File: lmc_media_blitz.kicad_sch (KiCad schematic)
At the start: 56 parts, among them J3 Conn_01x12, J4 Conn_01x12, Q1 BSS138W, Q2 BSS138W, SW1 SW_Push, SW2 SW_Push, SW3 SW_Push, U1 XC6206PxxxMR, U2 TPS613222ADBV, U3 STM32F030C8Tx

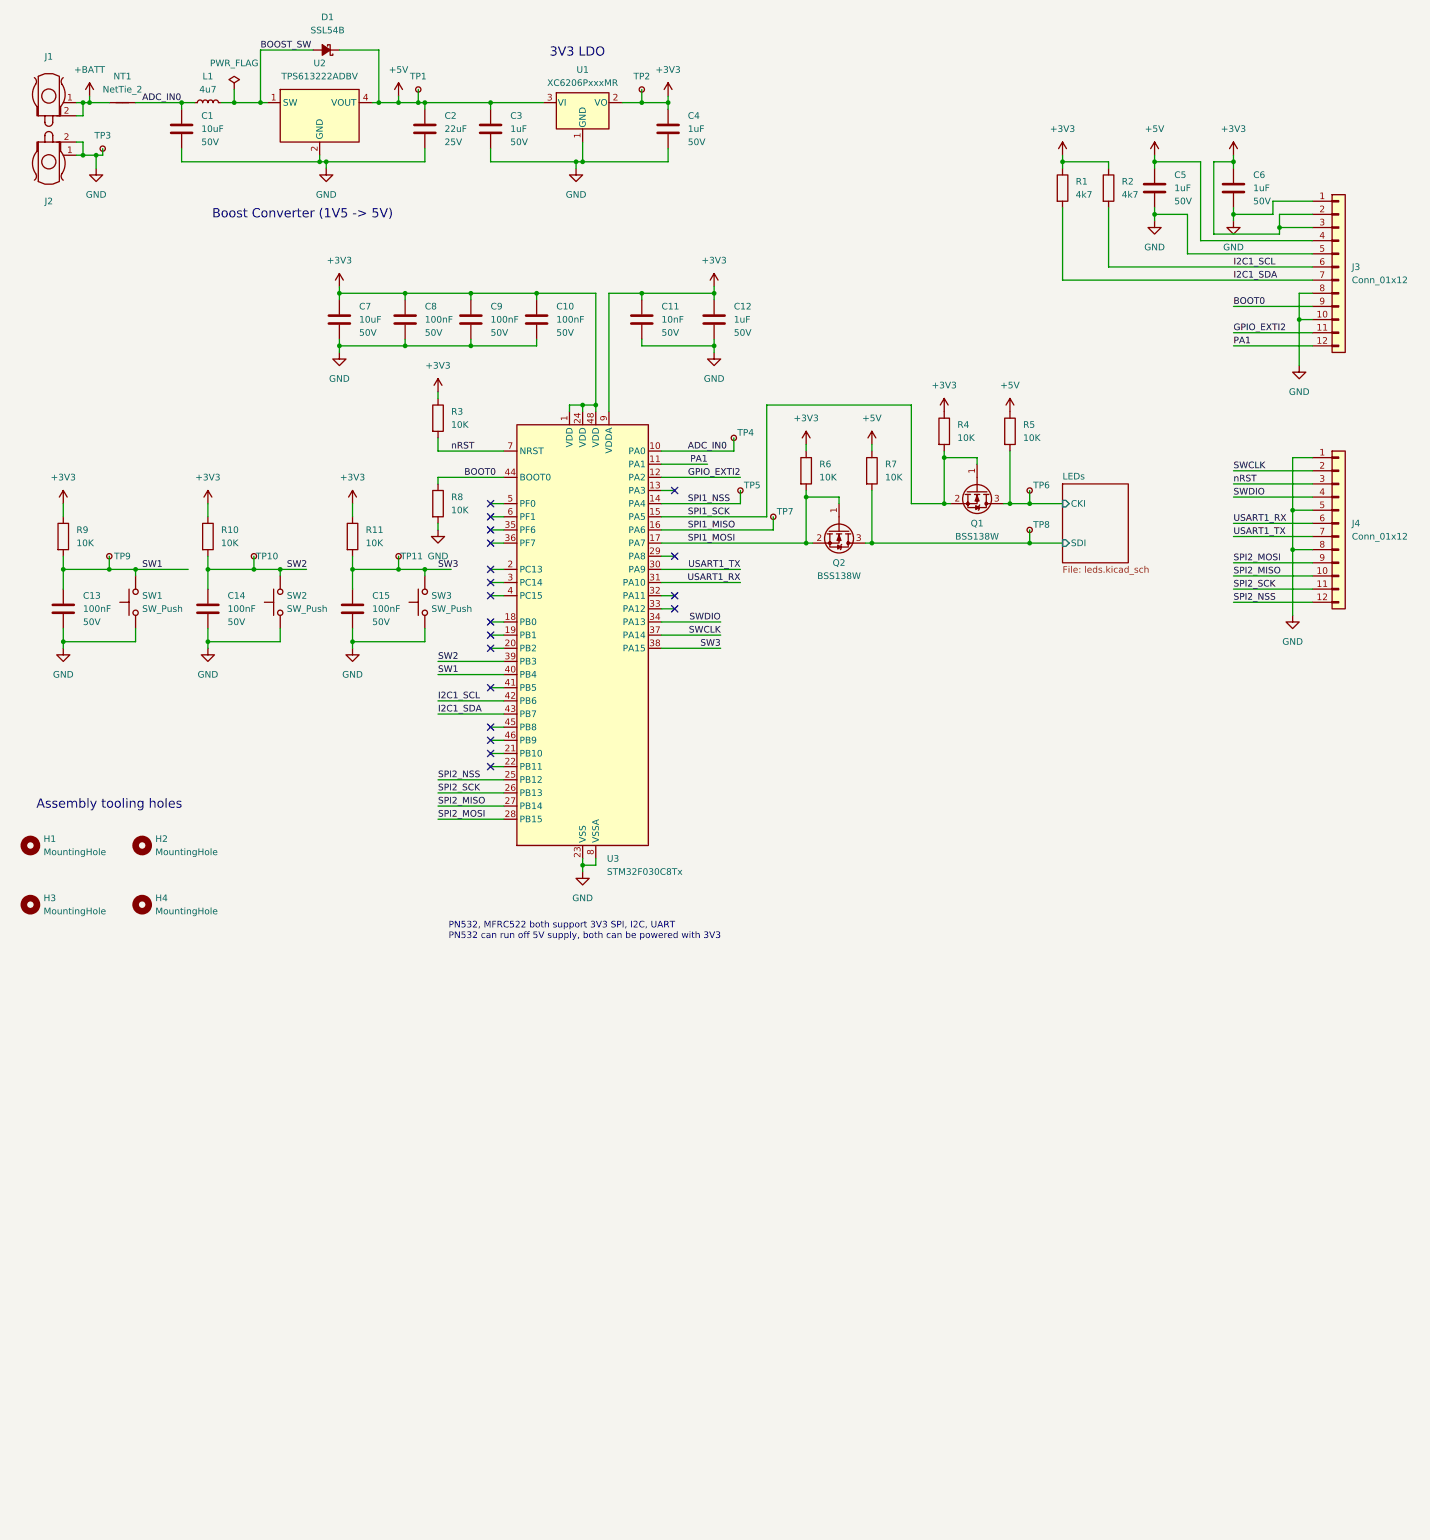
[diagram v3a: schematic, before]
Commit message: Changed 1x12 connectors to 2x12 connectors, and made board shape rectangular
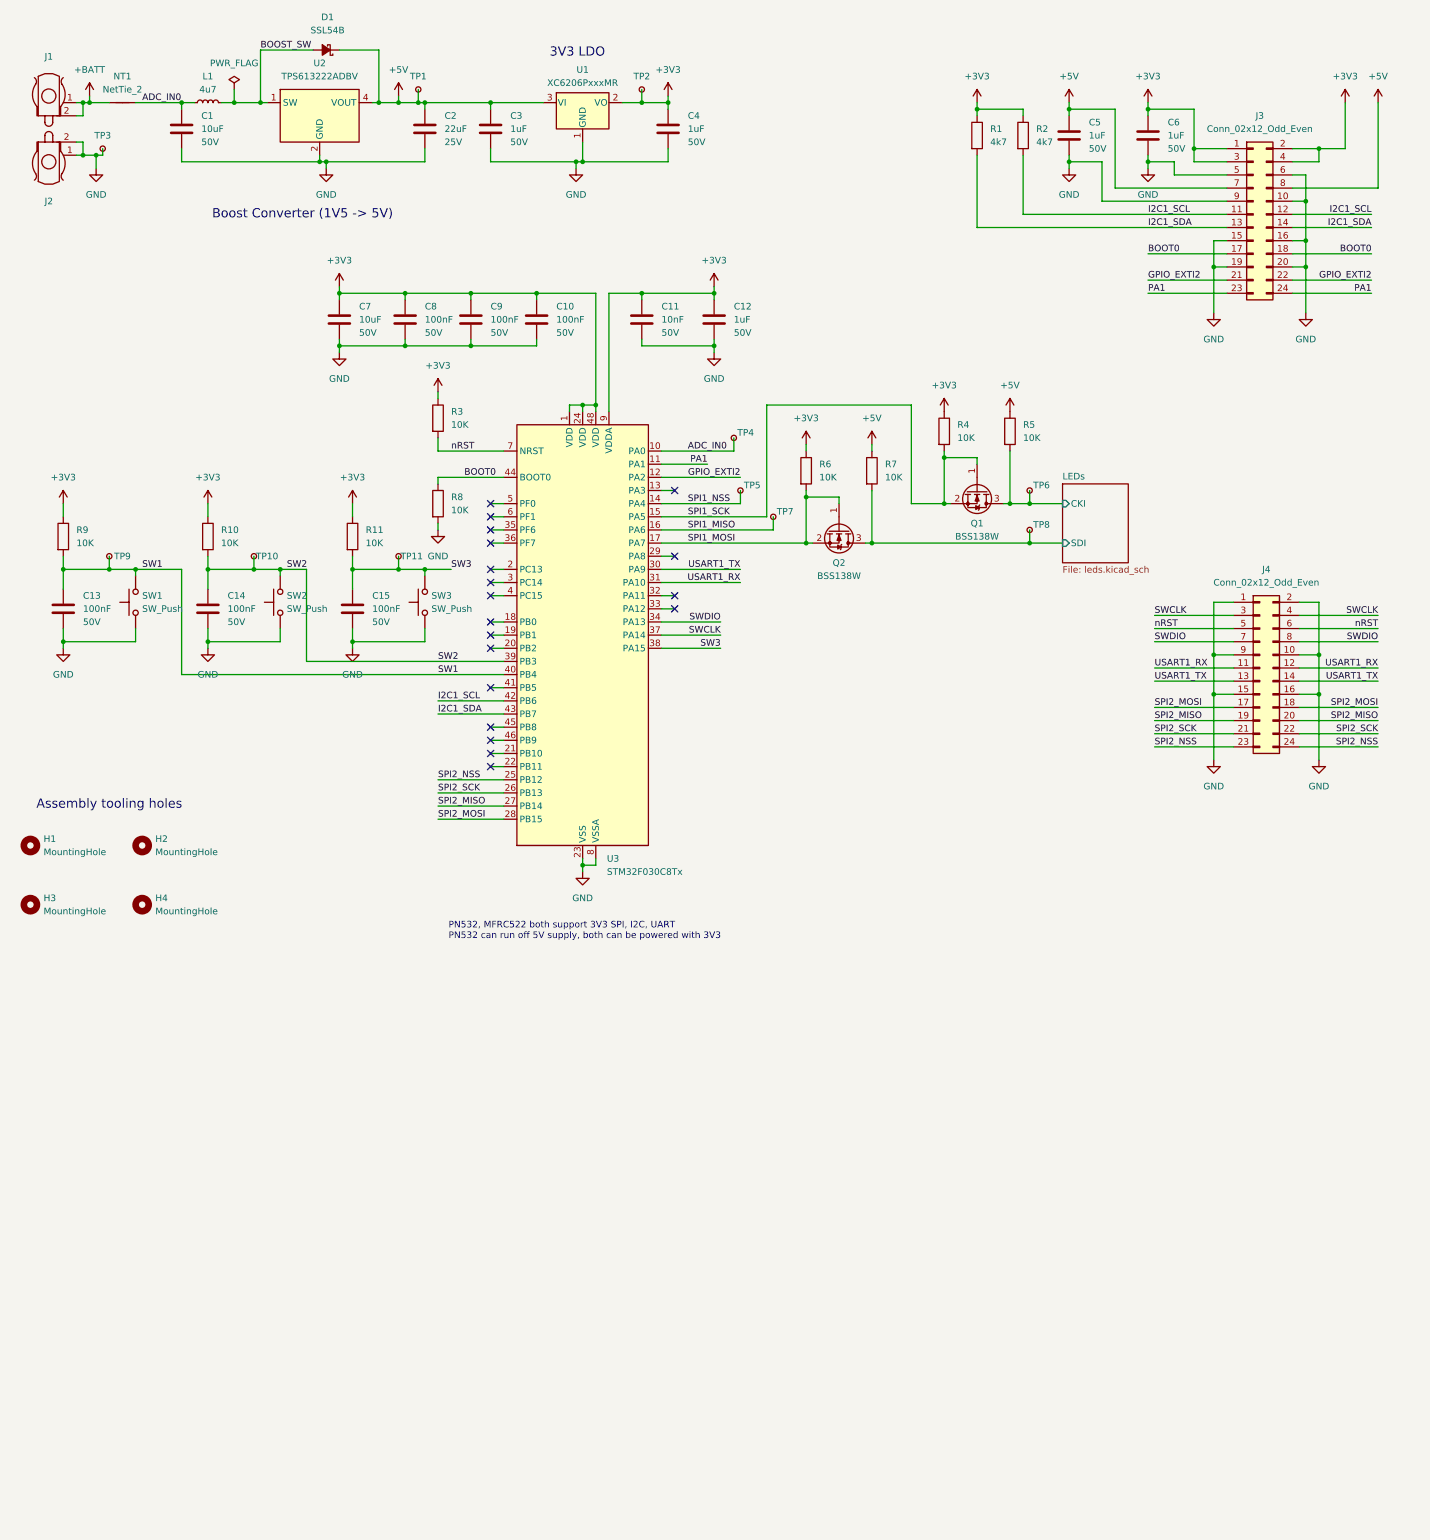
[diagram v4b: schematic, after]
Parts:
- removed J3, J4: Conn_01x12, Connector_PinSocket_2.54mm:PinSocket_1x12_P2.54mm_Vertical, symbol Connector_Generic:Conn_01x12
- added J3, J4: Conn_02x12_Odd_Even, Connector_PinHeader_2.54mm:PinHeader_2x12_P2.54mm_Vertical, symbol Connector_Generic:Conn_02x12_Odd_Even
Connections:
- net +3V3: now also J3.1 (Pin_1), J3.2 (Pin_2), J3.3 (Pin_3), J3.4 (Pin_4)
- net +5V: now also J3.7 (Pin_7), J3.8 (Pin_8)
- net BOOT0: now also J3.17 (Pin_17), J3.18 (Pin_18)
- net GND: now also J3.10 (Pin_10), J3.15 (Pin_15), J3.16 (Pin_16), J3.19 (Pin_19), J3.20 (Pin_20), J3.5 (Pin_5), J3.6 (Pin_6), J3.9 (Pin_9), J4.1 (Pin_1), J4.10 (Pin_10), J4.15 (Pin_15), J4.16 (Pin_16), J4.2 (Pin_2), J4.9 (Pin_9)
- net GPIO_EXTI2: now also J3.21 (Pin_21), J3.22 (Pin_22)
- net I2C1_SCL: now also J3.11 (Pin_11), J3.12 (Pin_12)
- net I2C1_SDA: now also J3.13 (Pin_13), J3.14 (Pin_14)
- net PA1: now also J3.23 (Pin_23), J3.24 (Pin_24)
- net SPI2_MISO: now also J4.19 (Pin_19), J4.20 (Pin_20)
- net SPI2_MOSI: now also J4.17 (Pin_17), J4.18 (Pin_18)
- net SPI2_NSS: now also J4.23 (Pin_23), J4.24 (Pin_24)
- net SPI2_SCK: now also J4.21 (Pin_21), J4.22 (Pin_22)
- net SWCLK: now also J4.3 (Pin_3), J4.4 (Pin_4)
- net SWDIO: now also J4.7 (Pin_7), J4.8 (Pin_8)
- net USART1_RX: now also J4.11 (Pin_11), J4.12 (Pin_12)
- net USART1_TX: now also J4.13 (Pin_13), J4.14 (Pin_14)
- net nRST: now also J4.5 (Pin_5), J4.6 (Pin_6)
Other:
- moved on the sheet: C5, C6, R1, R2
